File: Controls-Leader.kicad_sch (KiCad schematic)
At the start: 48 parts, among them J1 ExtraADCs, J13 UART_TP, J15 Conn_02x03_Odd_Even, J2 UART_TP, J25 UART_TP, J3 ExtraGPIO_Conn, J8 SWD, SW10 RESET, U7 STM32F413RHTx, Y1 Crystal

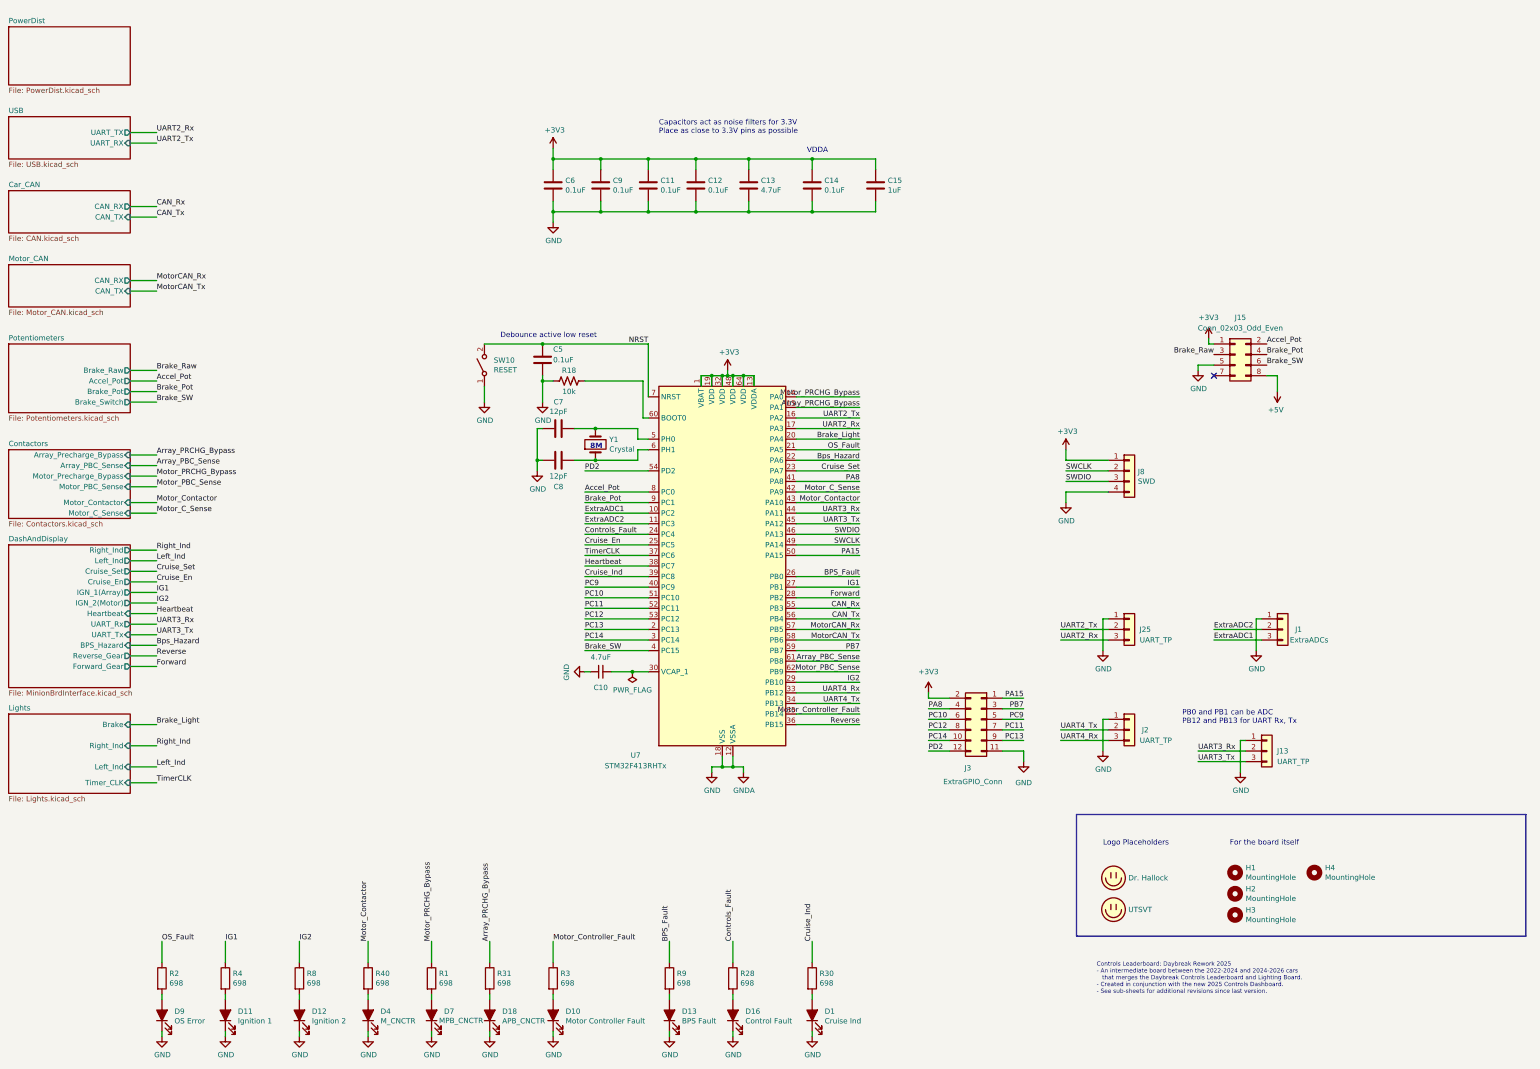
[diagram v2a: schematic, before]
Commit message: Fixed silkscreen issues from last version
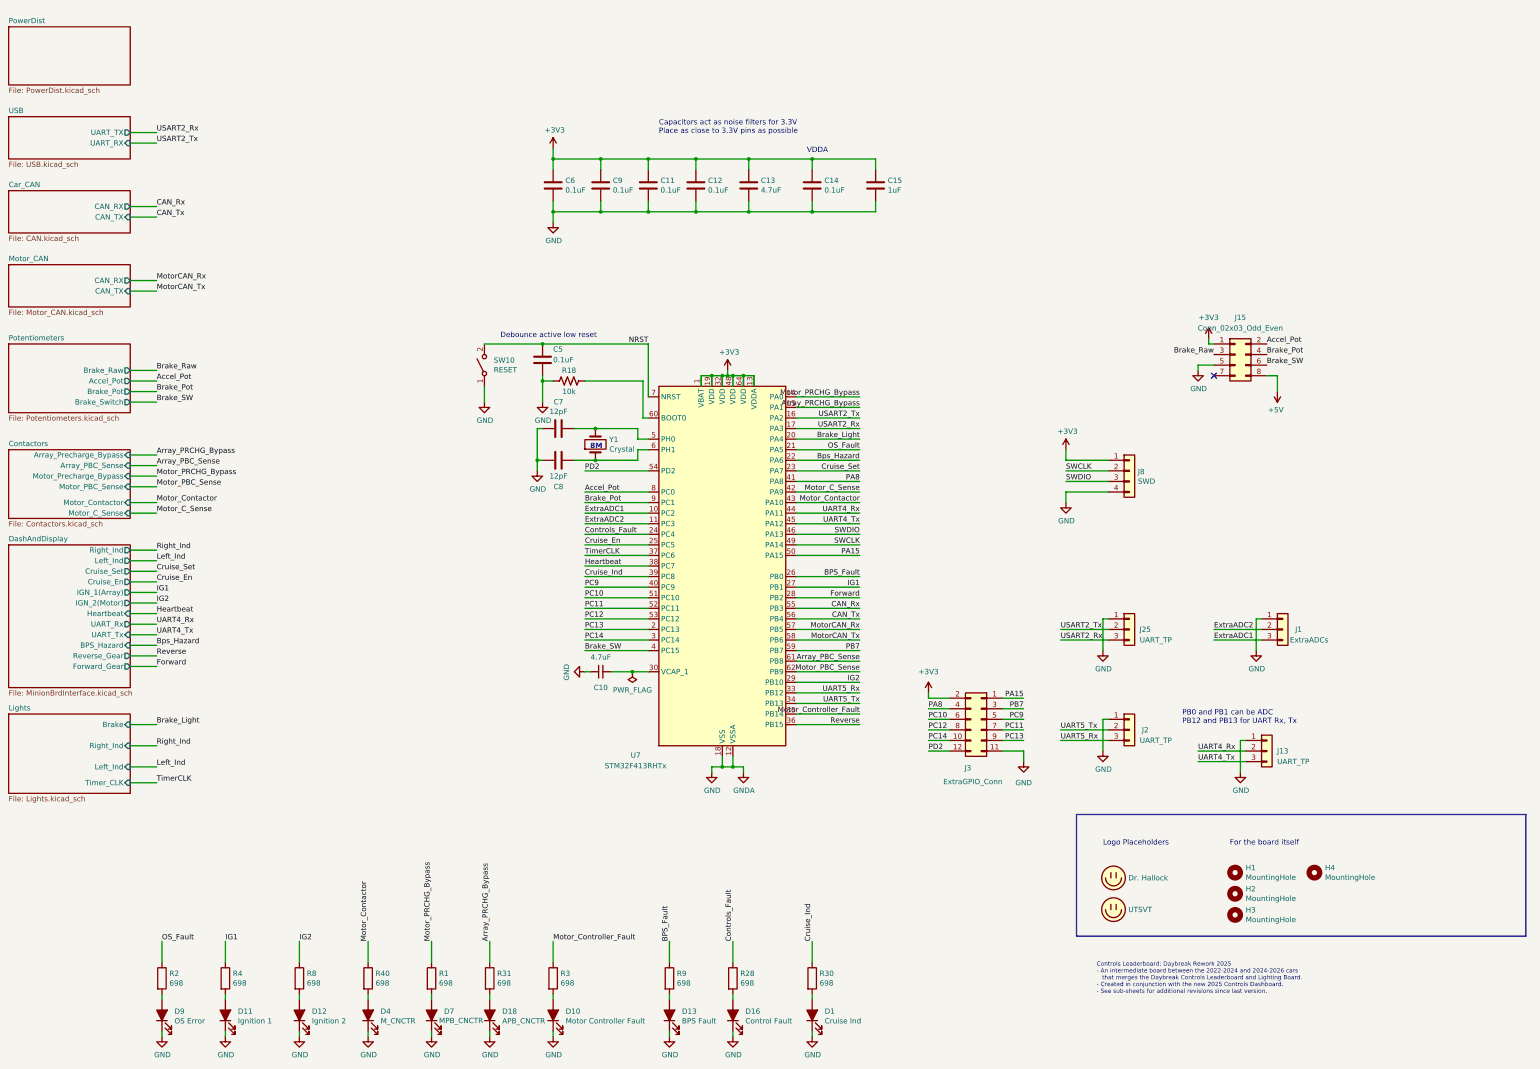
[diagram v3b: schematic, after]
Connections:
- net UART3_Rx is gone; now on net UART4_Rx: J13.2 (Pin_2), U7.44 (PA11)
- net UART3_Tx is gone; now on net UART4_Tx: J13.3 (Pin_3), U7.45 (PA12)
- net UART4_Rx: no longer J2.3 (Pin_3), U7.33 (PB12)
- net UART4_Tx: no longer J2.2 (Pin_2), U7.34 (PB13)
- net UART2_Rx renamed USART2_Rx
- net UART2_Tx renamed USART2_Tx
- new net UART5_Rx: J2.3 (Pin_3), U7.33 (PB12)
- new net UART5_Tx: J2.2 (Pin_2), U7.34 (PB13)
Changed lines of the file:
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@@
 		)
 	)
-	(label "UART4_Rx"
+	(label "UART5_Rx"
 		(at 292.1 200.66 0)
 		(fields_autoplaced yes)
@@
 		)
 	)
-	(label "UART2_Rx"
+	(label "USART2_Rx"
 		(at 243.84 125.73 180)
 		(fields_autoplaced yes)
@@
 		)
 	)
-	(label "UART3_Tx"
+	(label "UART4_Tx"
 		(at 243.84 148.59 180)
 		(fields_autoplaced yes)
@@
 		)
 	)
-	(label "UART2_Tx"
+	(label "USART2_Tx"
 		(at 243.84 123.19 180)
 		(fields_autoplaced yes)
@@
 		)
 	)
-	(label "UART2_Tx"
+	(label "USART2_Tx"
 		(at 292.1 173.99 0)
 		(fields_autoplaced yes)
@@
 		)
 	)
-	(label "UART4_Rx"
+	(label "UART5_Rx"
 		(at 243.84 189.23 180)
 		(fields_autoplaced yes)
@@
 		)
 	)
-	(label "UART3_Rx"
+	(label "UART4_Rx"
 		(at 325.12 203.2 0)
 		(fields_autoplaced yes)
@@
 		)
 	)
-	(label "UART2_Tx"
+	(label "USART2_Tx"
 		(at 74.93 57.15 0)
 		(fields_autoplaced yes)
@@
 		)
 	)
-	(label "UART2_Rx"
+	(label "USART2_Rx"
 		(at 74.93 54.61 0)
 		(fields_autoplaced yes)
@@
 		)
 	)
-	(label "UART2_Rx"
+	(label "USART2_Rx"
 		(at 292.1 176.53 0)
 		(fields_autoplaced yes)
@@
 		)
 	)
-	(label "UART3_Tx"
+	(label "UART4_Tx"
 		(at 74.93 175.26 0)
 		(fields_autoplaced yes)
@@
 		)
 	)
-	(label "UART3_Rx"
+	(label "UART4_Rx"
 		(at 243.84 146.05 180)
 		(fields_autoplaced yes)
@@
 		)
 	)
-	(label "UART4_Tx"
+	(label "UART5_Tx"
 		(at 243.84 191.77 180)
 		(fields_autoplaced yes)
@@
 		)
 	)
-	(label "UART4_Tx"
+	(label "UART5_Tx"
 		(at 292.1 198.12 0)
 		(fields_autoplaced yes)
@@
 		)
 	)
-	(label "UART3_Rx"
+	(label "UART4_Rx"
 		(at 74.93 172.72 0)
 		(fields_autoplaced yes)
@@
 		)
 	)
-	(label "UART3_Tx"
+	(label "UART4_Tx"
 		(at 325.12 205.74 0)
 		(fields_autoplaced yes)

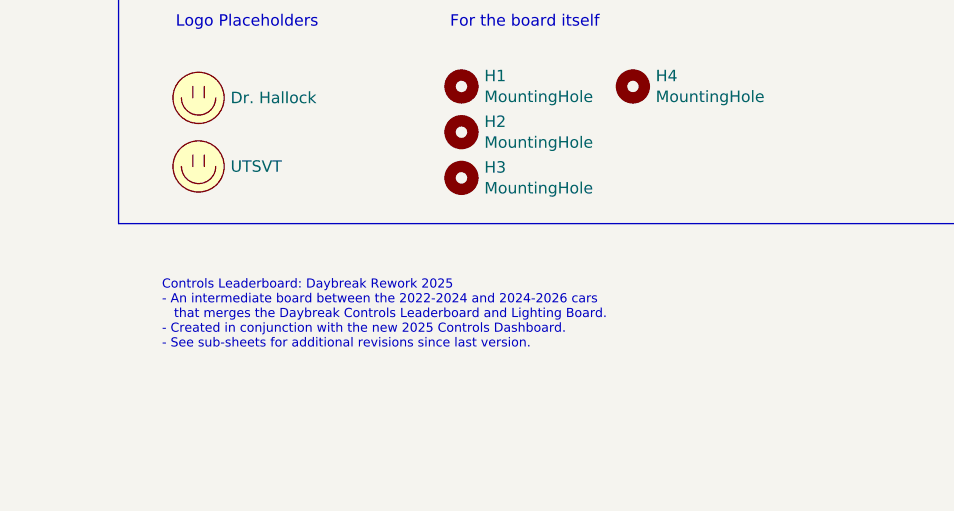
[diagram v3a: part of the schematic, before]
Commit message: Added 3D view and schematic pdf.
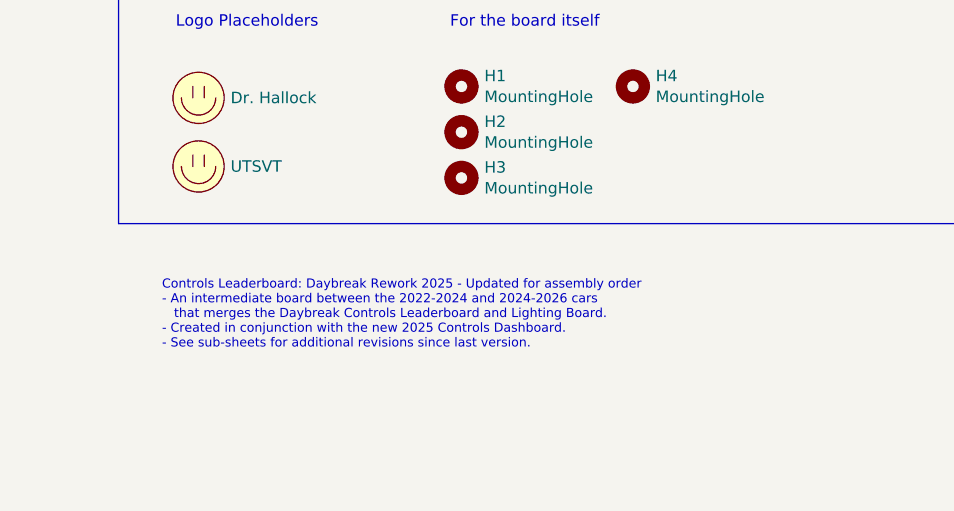
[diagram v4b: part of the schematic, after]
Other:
- note added: "Controls Leaderboard: Daybreak Rework 2025 - Updated for assembly order - An intermediate board between the 2022-2024 and 2024-2026 cars that merges the Daybreak Controls Leaderboard and Lighting Board. - Created in conjunction with the new 2025 Controls Dashboard. - See sub-sheets for additional revisions since last version."
- note removed: "Controls Leaderboard: Daybreak Rework 2025 - An intermediate board between the 2022-2024 and 2024-2026 cars that merges the Daybreak Controls Leaderboard and Lighting Board. - Created in conjunction with the new 2025 Controls Dashboard. - See sub-sheets for additional revisions since last version."
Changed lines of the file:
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@@
 		)
 	)
-	(text "Controls Leaderboard: Daybreak Rework 2025\n- An intermediate board between the 2022-2024 and 2024-2026 cars\n   that merges the Daybreak Controls Leaderboard and Lighting Board.\n- Created in conjunction with the new 2025 Controls Dashboard.\n- See sub-sheets for additional revisions since last version."
+	(text "Controls Leaderboard: Daybreak Rework 2025 - Updated for assembly order\n- An intermediate board between the 2022-2024 and 2024-2026 cars\n   that merges the Daybreak Controls Leaderboard and Lighting Board.\n- Created in conjunction with the new 2025 Controls Dashboard.\n- See sub-sheets for additional revisions since last version."
 		(exclude_from_sim no)
 		(at 300.736 257.81 0)
